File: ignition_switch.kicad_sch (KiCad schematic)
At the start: 9 parts, among them J9 POW_2ND_CONN, SW8 SW_Rotary2x6, U5 EL3H7, U6 EL3H7

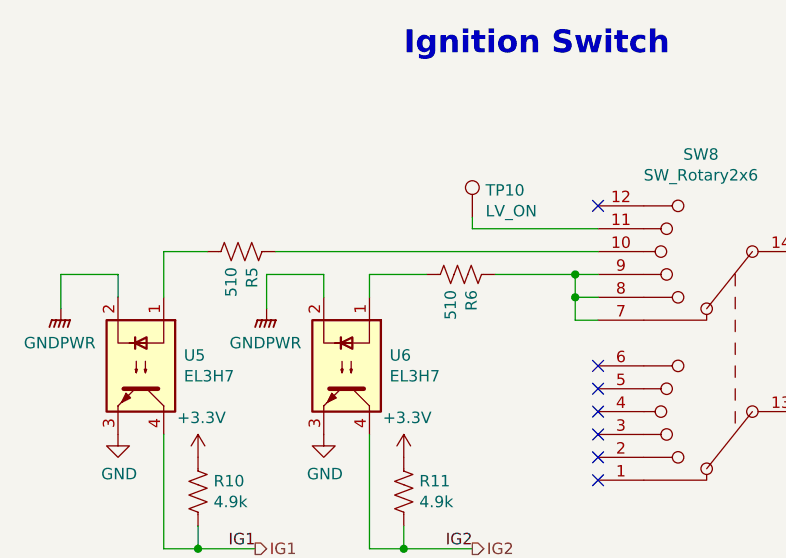
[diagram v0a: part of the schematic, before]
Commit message: changed resistor values, updated footprints
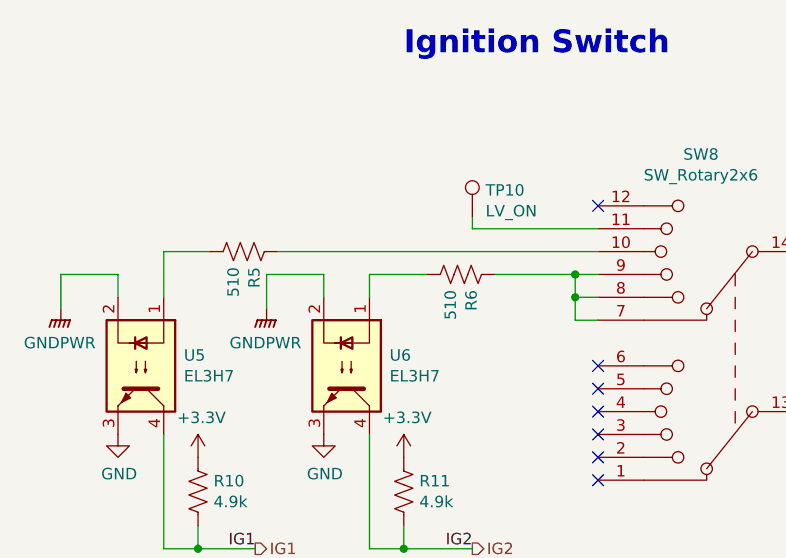
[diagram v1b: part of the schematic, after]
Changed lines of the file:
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@@
+    (stroke (width 0) (type default))
+  )
+  (wire (pts (xy 101.6 76.2) (xy 137.16 76.2))
     (stroke (width 0) (type default))
   )
@@
     (stroke (width 0) (type default))
   )
-  (wire (pts (xy 101.346 76.2) (xy 137.16 76.2))
+  (wire (pts (xy 88.9 76.2) (xy 93.98 76.2))
     (stroke (width 0) (type default))
   )
@@
   )
   (wire (pts (xy 111.76 109.22) (xy 115.57 109.22))
-    (stroke (width 0) (type default))
-  )
-  (wire (pts (xy 88.9 76.2) (xy 93.726 76.2))
     (stroke (width 0) (type default))
   )
@@
     )
   )
-  (symbol (lib_id "Device:R_US") (at 97.536 76.2 270) (unit 1)
-    (in_bom yes) (on_board yes) (dnp no)
-    (property "Reference" "R5" (at 98.7044 77.9272 0)
-      (effects (font (size 1.27 1.27)) (justify left))
-    )
-    (property "Value" "510" (at 96.393 77.9272 0)
-      (effects (font (size 1.27 1.27)) (justify left))
-    )
-    (property "Footprint" "Resistor_SMD:R_0805_2012Metric" (at 97.282 77.216 90)
-      (effects (font (size 1.27 1.27)) hide)
-    )
-    (property "Datasheet" "~" (at 97.536 76.2 0)
-      (effects (font (size 1.27 1.27)) hide)
-    )
-    (property "Mouser Part Number" "71-CRCW08054K99FKEAC " (at 97.536 76.2 0)
-      (effects (font (size 1.27 1.27)) hide)
-    )
+  (symbol (lib_id "Device:R_US") (at 97.79 76.2 270) (unit 1)
+    (in_bom yes) (on_board yes) (dnp no)
+    (property "Reference" "R5" (at 98.9584 77.9272 0)
+      (effects (font (size 1.27 1.27)) (justify left))
+    )
+    (property "Value" "510" (at 96.647 77.9272 0)
+      (effects (font (size 1.27 1.27)) (justify left))
+    )
+    (property "Footprint" "Resistor_SMD:R_0805_2012Metric" (at 97.536 77.216 90)
+      (effects (font (size 1.27 1.27)) hide)
+    )
+    (property "Datasheet" "~" (at 97.79 76.2 0)
+      (effects (font (size 1.27 1.27)) hide)
+    )
+    (property "Mouser Part Number" "71-CRCW08054K99FKEAC " (at 97.79 76.2 0)
+      (effects (font (size 1.27 1.27)) hide)
+    )

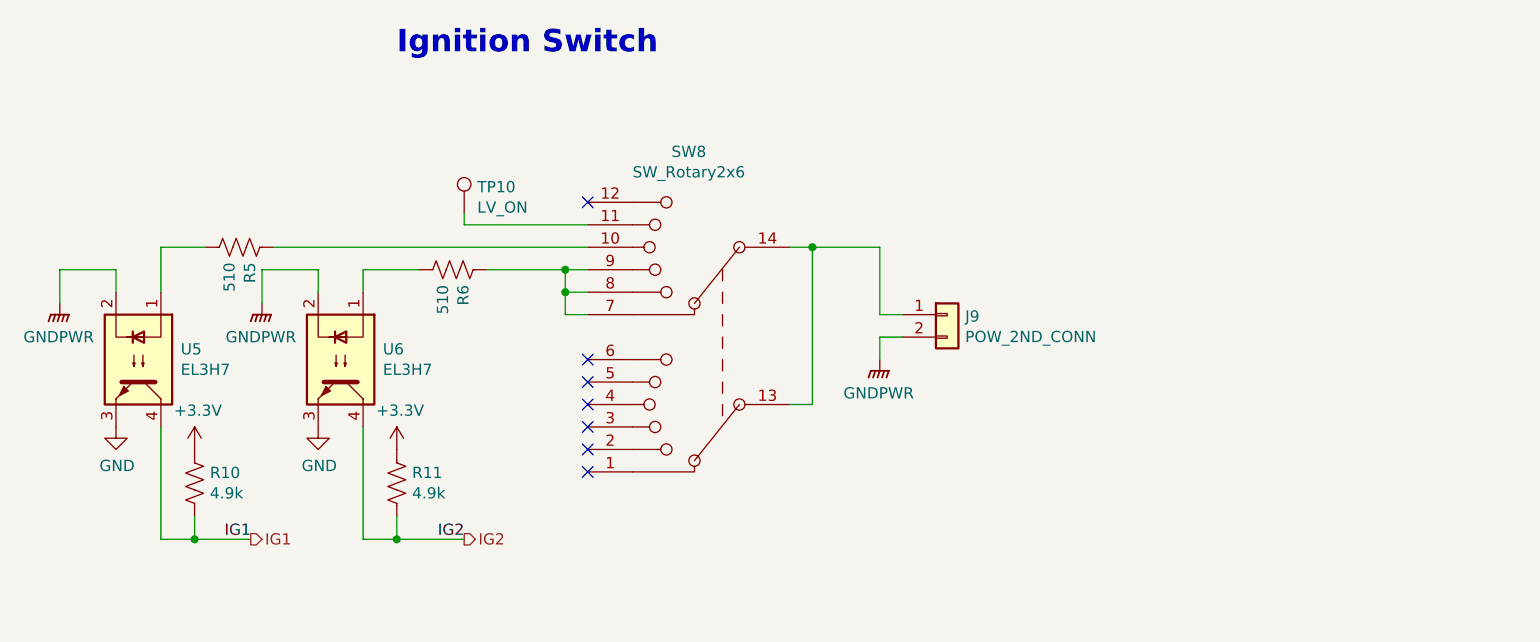
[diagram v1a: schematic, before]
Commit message: Added resistor to fan isolator, fixed ERC errors and warnings
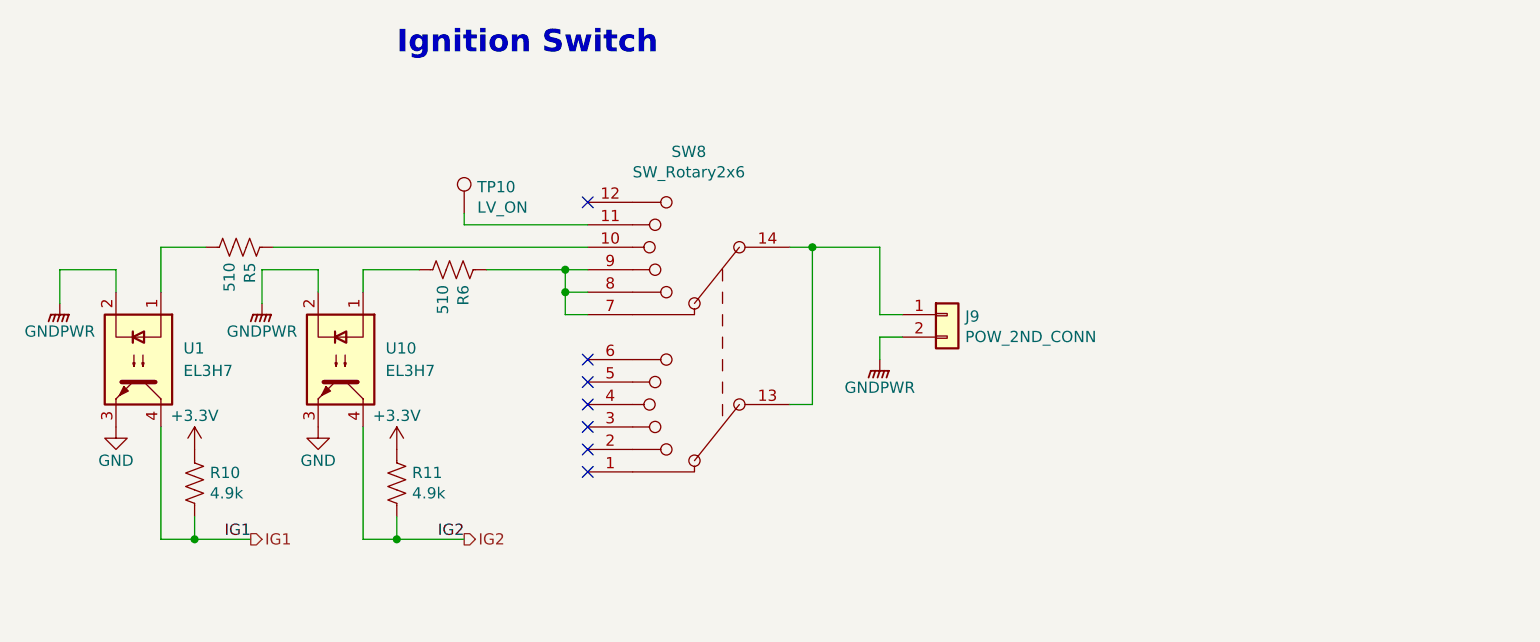
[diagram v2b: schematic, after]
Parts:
- removed U5, U6: EL3H7, Package_SO:SOP-4_4.4x2.6mm_P1.27mm, symbol Isolator:SFH617A-1
- added U1, U10: EL3H7, Package_SO:SOP-4_4.4x2.6mm_P1.27mm, symbol Isolator:EL817
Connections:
- net GND: now also U1.3, U10.3
- net GNDPWR: now also U1.2, U10.2
- net IG1: now also U1.4
- net IG2: now also U10.4
- net at R5.2: now also U1.1
- net at R6.2: now also U10.1
- net +3V3 renamed +3.3V

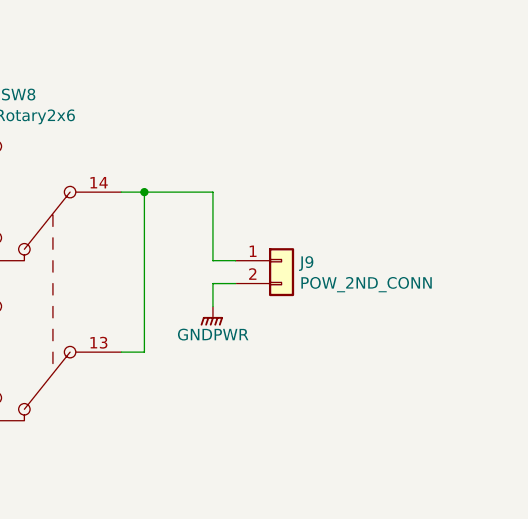
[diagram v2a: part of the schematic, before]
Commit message: changed labels for some connectors
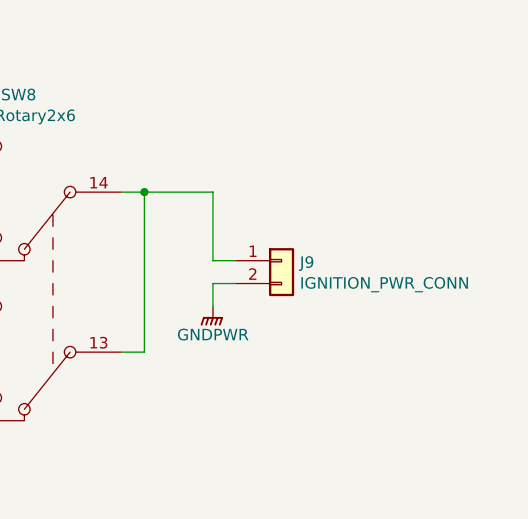
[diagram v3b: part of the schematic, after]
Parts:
- J9: value POW_2ND_CONN -> IGNITION_PWR_CONN
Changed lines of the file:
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@@
       (effects (font (size 1.27 1.27)) (justify left))
     )
-    (property "Value" "POW_2ND_CONN" (at 179.832 86.3346 0)
+    (property "Value" "IGNITION_PWR_CONN" (at 179.832 86.3346 0)
       (effects (font (size 1.27 1.27)) (justify left))
     )
@@
       (project "Controls-DaughterPCB"
         (path "/c7871779-04fe-4705-8150-20a4dd0ef44f/0d7b9330-5178-458e-b803-9c8d464fd559"
-          (reference "J4") (unit 1)
+          (reference "IG_PWR1") (unit 1)
         )
       )

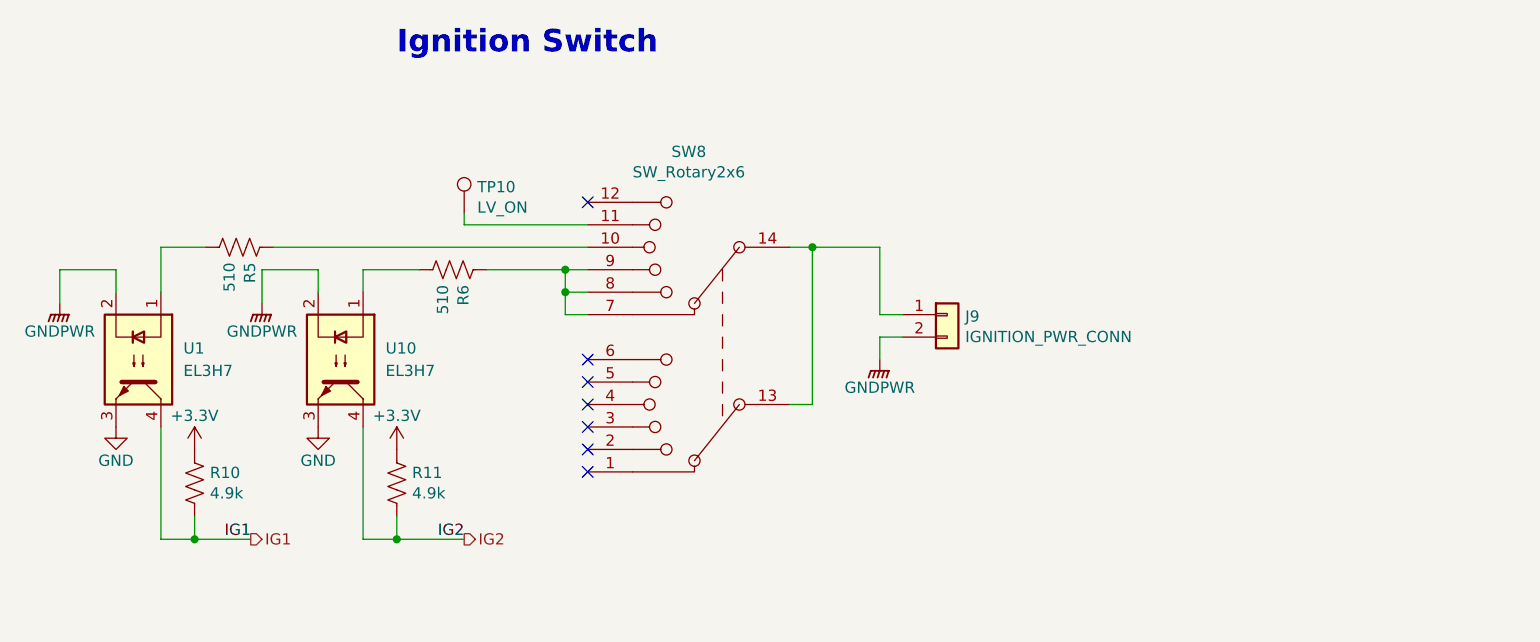
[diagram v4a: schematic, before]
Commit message: Removed ignition switch connection and redid ignition signals
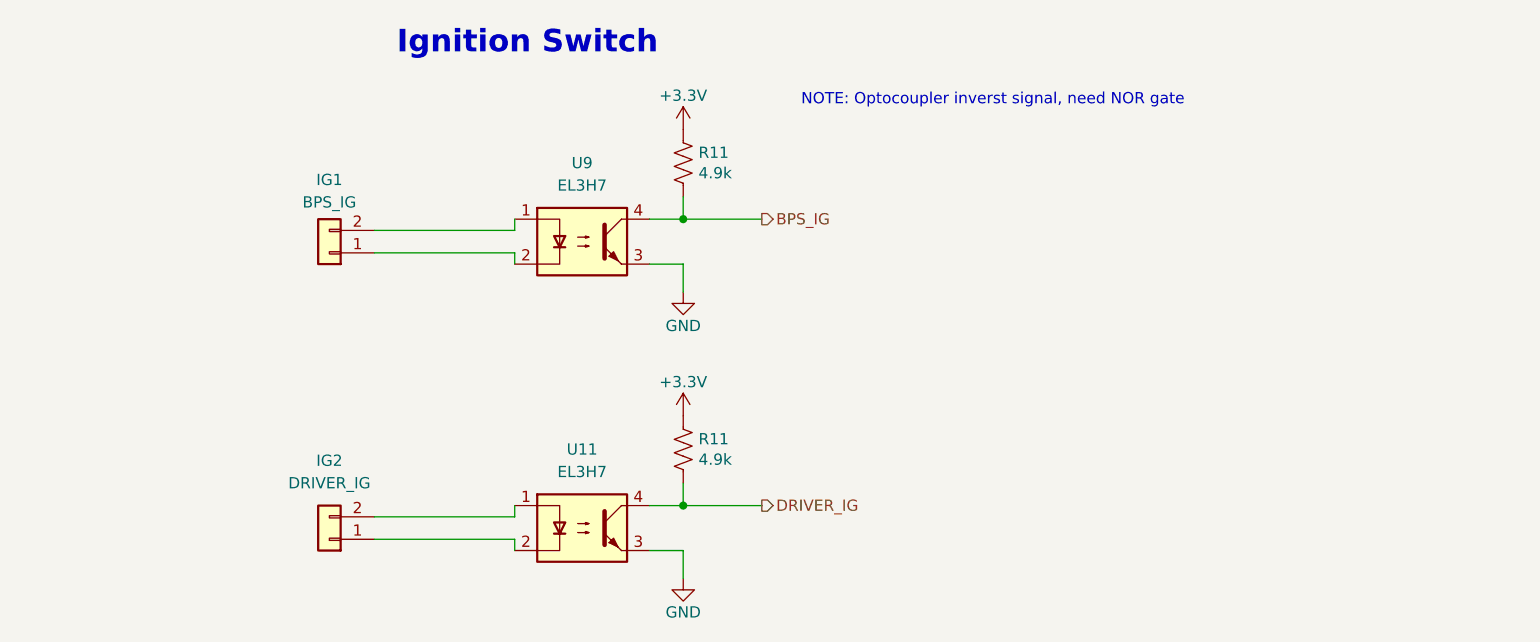
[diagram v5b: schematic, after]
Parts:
- removed J9: IGNITION_PWR_CONN, UTSVT_Connectors:Molex_MicroFit3.0_1x2xP3.00mm_PolarizingPeg_Vertical, symbol Connector_Generic:Conn_01x02
- removed R10, R11: 4.9k, Resistor_SMD:R_0805_2012Metric, symbol Device:R_US
- removed R5, R6: 510, Resistor_SMD:R_0805_2012Metric, symbol Device:R_US
- removed SW8: SW_Rotary2x6, Connector_Molex:Molex_Micro-Fit_3.0_43045-1412_2x07_P3.00mm_Vertical, symbol Switch:SW_Rotary2x6
- removed TP10: LV_ON, TestPoint:TestPoint_Pad_1.5x1.5mm, symbol Connector:TestPoint
- removed U1, U10: EL3H7, Package_SO:SOP-4_4.4x2.6mm_P1.27mm, symbol Isolator:EL817
- added IG1: BPS_IG, symbol Connector_Generic:Conn_01x02
- added IG2: DRIVER_IG, symbol Connector_Generic:Conn_01x02
- added R11 (x2): 4.9k, Resistor_SMD:R_0805_2012Metric, symbol Device:R_US
- added U11, U9: EL3H7, Package_SO:SOP-4_4.4x2.6mm_P1.27mm, symbol Isolator:EL817
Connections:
- net +3.3V: now also R11.1, R11.1
- net GND: now also U11.3, U9.3
- new net: IG1.1 (Pin_1), U9.2
- new net: IG1.2 (Pin_2), U9.1
- new net: IG2.2 (Pin_2), U11.1
- new net: IG2.1 (Pin_1), U11.2
- new net BPS_IG: R11.2, U9.4
- new net DRIVER_IG: R11.2, U11.4
- no-connect marks 7 -> 0
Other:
- note added: "NOTE: Optocoupler inverst signal, need NOR gate"

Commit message: updated footprints and part numbers, added motor CAN 12V connection
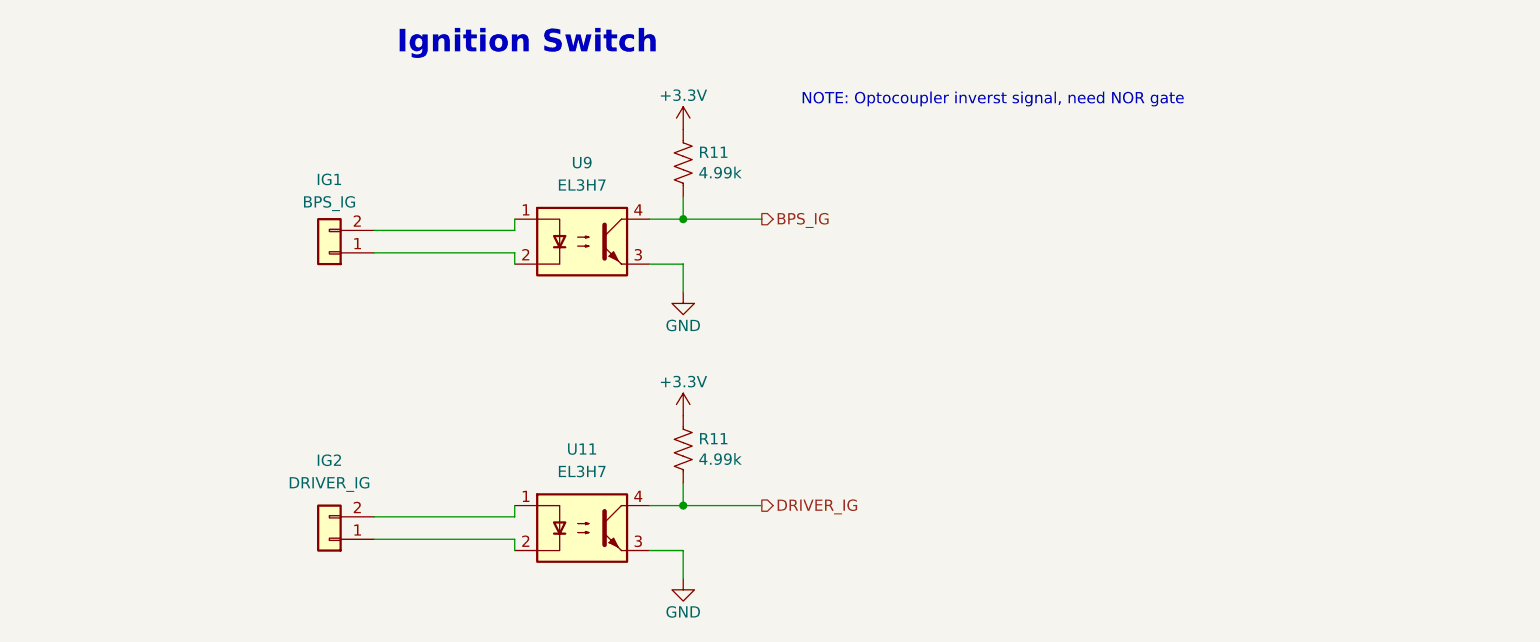
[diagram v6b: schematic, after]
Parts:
- IG1, IG2: footprint (none) -> Connector_Molex:Molex_Micro-Fit_3.0_43650-0215_1x02_P3.00mm_Vertical; PN (none) -> 43650-0215
- R11: value 4.9k -> 4.99k; Mauser PN (none) -> 71-CRCW08054K99FKEAC; Mouser Part Number 71-CRCW08054K99FKEAC -> (none); PN (none) -> CRCW08054K99FKEAC
- U11, U9: Mauser PN (none) -> 638-EL3H7DTAVG; Mouser Part Number 638-EL3H7DTAVG -> (none); PN (none) -> EL3H7(D)(TA)-VG
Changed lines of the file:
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@@
       (effects (font (size 1.27 1.27)))
     )
-    (property "Footprint" "" (at 107.95 76.835 0)
-      (effects (font (size 1.27 1.27)) hide)
-    )
-    (property "Datasheet" "~" (at 107.95 76.835 0)
+    (property "Footprint" "Connector_Molex:Molex_Micro-Fit_3.0_43650-0215_1x02_P3.00mm_Vertical" (at 107.95 76.835 0)
+      (effects (font (size 1.27 1.27)) hide)
+    )
+    (property "Datasheet" "https://www.molex.com/content/dam/molex/molex-dot-com/products/automated/en-us/productspecificationpdf/436/43650/PS-43650-001.pdf?inline" (at 107.95 76.835 0)
+      (effects (font (size 1.27 1.27)) hide)
+    )
+    (property "PN" "43650-0215" (at 107.95 76.835 0)
       (effects (font (size 1.27 1.27)) hide)
     )
@@
       (effects (font (size 1.27 1.27)) (justify left) hide)
     )
-    (property "Mouser Part Number" "638-EL3H7DTAVG " (at 136.525 107.95 90)
+    (property "Mauser PN" "638-EL3H7DTAVG " (at 136.525 107.95 0)
+      (effects (font (size 1.27 1.27)) hide)
+    )
+    (property "PN" "EL3H7(D)(TA)-VG" (at 136.525 107.95 0)
       (effects (font (size 1.27 1.27)) hide)
     )
@@
       (effects (font (size 1.27 1.27)) (justify left) hide)
     )
-    (property "Mouser Part Number" "638-EL3H7DTAVG " (at 136.525 75.565 90)
+    (property "Mauser PN" "638-EL3H7DTAVG " (at 136.525 75.565 0)
+      (effects (font (size 1.27 1.27)) hide)
+    )
+    (property "PN" "EL3H7(D)(TA)-VG" (at 136.525 75.565 0)
       (effects (font (size 1.27 1.27)) hide)
     )
@@
       (effects (font (size 1.27 1.27)))
     )
-    (property "Footprint" "" (at 107.95 109.22 0)
-      (effects (font (size 1.27 1.27)) hide)
-    )
-    (property "Datasheet" "~" (at 107.95 109.22 0)
+    (property "Footprint" "Connector_Molex:Molex_Micro-Fit_3.0_43650-0215_1x02_P3.00mm_Vertical" (at 107.95 109.22 0)
+      (effects (font (size 1.27 1.27)) hide)
+    )
+    (property "Datasheet" "https://www.molex.com/content/dam/molex/molex-dot-com/products/automated/en-us/productspecificationpdf/436/43650/PS-43650-001.pdf?inline" (at 107.95 109.22 0)
+      (effects (font (size 1.27 1.27)) hide)
+    )
+    (property "PN" "43650-0215" (at 107.95 109.22 0)
       (effects (font (size 1.27 1.27)) hide)
     )
@@
       (effects (font (size 1.27 1.27)) (justify left))
     )
-    (property "Value" "4.9k" (at 149.6822 67.818 0)
+    (property "Value" "4.99k" (at 149.6822 67.818 0)
       (effects (font (size 1.27 1.27)) (justify left))
     )
@@
       (effects (font (size 1.27 1.27)) hide)
     )
-    (property "Datasheet" "~" (at 147.955 66.675 0)
-      (effects (font (size 1.27 1.27)) hide)
-    )
-    (property "Mouser Part Number" "71-CRCW08054K99FKEAC " (at 147.955 66.675 0)
+    (property "Datasheet" "https://www.vishay.com/docs/28773/crcwce3.pdf" (at 147.955 66.675 0)
+      (effects (font (size 1.27 1.27)) hide)
+    )
+    (property "PN" "CRCW08054K99FKEAC" (at 147.955 66.675 0)
+      (effects (font (size 1.27 1.27)) hide)
+    )
+    (property "Mauser PN" "71-CRCW08054K99FKEAC " (at 147.955 66.675 0)
       (effects (font (size 1.27 1.27)) hide)
     )
@@
       (effects (font (size 1.27 1.27)) (justify left))
     )
-    (property "Value" "4.9k" (at 149.6822 100.203 0)
+    (property "Value" "4.99k" (at 149.6822 100.203 0)
       (effects (font (size 1.27 1.27)) (justify left))
     )
@@
       (effects (font (size 1.27 1.27)) hide)
     )
-    (property "Datasheet" "~" (at 147.955 99.06 0)
-      (effects (font (size 1.27 1.27)) hide)
-    )
-    (property "Mouser Part Number" "71-CRCW08054K99FKEAC " (at 147.955 99.06 0)
-      (effects (font (size 1.27 1.27)) hide)
-    )
+    (property "Datasheet" "https://www.vishay.com/docs/28773/crcwce3.pdf" (at 147.955 99.06 0)
+      (effects (font (size 1.27 1.27)) hide)
+    )
+    (property "PN" "CRCW08054K99FKEAC" (at 147.955 99.06 0)
+      (effects (font (size 1.27 1.27)) hide)
+    )
+    (property "Mauser PN" "71-CRCW08054K99FKEAC " (at 147.955 99.06 0)
+      (effects (font (size 1.27 1.27)) hide)
+    )
